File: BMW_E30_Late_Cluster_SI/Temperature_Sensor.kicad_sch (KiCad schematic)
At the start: 30 parts, among them Q11 BC327-16, Q12 BC337-25, Q13 BC337-16, Q14 BC547B, Q15 BC557B, Q17 BC337-25

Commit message: Improved Schematic Readability for SI Board
Added final trace flags for readability of the main page. Also exported a BOM for the SI board
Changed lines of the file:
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@@
 		)
 	)
-	(global_label "IC1_P17"
+	(hierarchical_label "IC1_P19"
 		(shape output)
-		(at 128.27 43.18 0)
-		(fields_autoplaced yes)
+		(at 128.27 57.15 0)
 		(effects
 			(font
@@
 			(justify left)
 		)
-		(property "Intersheetrefs" "${INTERSHEET_REFS}"
-			(at 138.9961 43.18 0)
-			(effects
-				(font
-					(size 1.27 1.27)
-				)
-				(justify left)
-				(hide yes)
+	)
+	(hierarchical_label "IC1_P18"
+		(shape bidirectional)
+		(at 251.46 67.31 0)
+		(effects
+			(font
+				(size 1.27 1.27)
 			)
+			(justify left)
 		)
 	)
-	(global_label "Eng_temp_sensor"
+	(hierarchical_label "Temp_GND"
+		(shape output)
+		(at 124.46 157.48 0)
+		(effects
+			(font
+				(size 1.27 1.27)
+			)
+			(justify left)
+		)
+	)
+	(hierarchical_label "IC1_P23"
+		(shape output)
+		(at 251.46 140.97 0)
+		(effects
+			(font
+				(size 1.27 1.27)
+			)
+			(justify left)
+		)
+	)
+	(hierarchical_label "Temp_+Ub"
+		(shape output)
+		(at 124.46 146.05 0)
+		(effects
+			(font
+				(size 1.27 1.27)
+			)
+			(justify left)
+		)
+	)
+	(hierarchical_label "Eng_temp_sensor"
 		(shape input)
 		(at 68.58 43.18 180)
-		(fields_autoplaced yes)
 		(effects
 			(font
@@
 			(justify right)
 		)
-		(property "Intersheetrefs" "${INTERSHEET_REFS}"
-			(at 49.327 43.18 0)
-			(effects
-				(font
-					(size 1.27 1.27)
-				)
-				(justify right)
-				(hide yes)
-			)
-		)
 	)
-	(global_label "IC1_P18"
+	(hierarchical_label "IC1_P18"
 		(shape input)
 		(at 39.37 148.59 180)
-		(fields_autoplaced yes)
 		(effects
 			(font
@@
 			(justify right)
 		)
-		(property "Intersheetrefs" "${INTERSHEET_REFS}"
-			(at 28.6439 148.59 0)
-			(effects
-				(font
-					(size 1.27 1.27)
-				)
-				(justify right)
-				(hide yes)
-			)
-		)
 	)
-	(global_label "IC3_P7"
-		(shape input)
+	(hierarchical_label "IC3_P7"
+		(shape output)
 		(at 251.46 115.57 0)
-		(fields_autoplaced yes)
 		(effects
 			(font
@@
 			(justify left)
 		)
-		(property "Intersheetrefs" "${INTERSHEET_REFS}"
-			(at 260.9766 115.57 0)
-			(effects
-				(font
-					(size 1.27 1.27)
-				)
-				(justify left)
-				(hide yes)
-			)
-		)
 	)
-	(global_label "IC1_P23"
-		(shape input)
-		(at 251.46 140.97 0)
-		(fields_autoplaced yes)
+	(hierarchical_label "IC1_P17"
+		(shape output)
+		(at 128.27 43.18 0)
 		(effects
 			(font
@@
 			(justify left)
 		)
-		(property "Intersheetrefs" "${INTERSHEET_REFS}"
-			(at 262.1861 140.97 0)
-			(effects
-				(font
-					(size 1.27 1.27)
-				)
-				(justify left)
-				(hide yes)
-			)
-		)
 	)
-	(global_label "IC1_P18"
-		(shape input)
-		(at 251.46 67.31 0)
-		(fields_autoplaced yes)
-		(effects
-			(font
-				(size 1.27 1.27)
-			)
-			(justify left)
-		)
-		(property "Intersheetrefs" "${INTERSHEET_REFS}"
-			(at 262.1861 67.31 0)
-			(effects
-				(font
-					(size 1.27 1.27)
-				)
-				(justify left)
-				(hide yes)
-			)
-		)
-	)
-	(global_label "Temp_+Ub"
-		(shape output)
-		(at 124.46 146.05 0)
-		(fields_autoplaced yes)
-		(effects
-			(font
-				(size 1.27 1.27)
-			)
-			(justify left)
-		)
-		(property "Intersheetrefs" "${INTERSHEET_REFS}"
-			(at 137.3632 146.05 0)
-			(effects
-				(font
-					(size 1.27 1.27)
-				)
-				(justify left)
-				(hide yes)
-			)
-		)
-	)
-	(global_label "Temp_GND"
-		(shape output)
-		(at 124.46 157.48 0)
-		(fields_autoplaced yes)
-		(effects
-			(font
-				(size 1.27 1.27)
-			)
-			(justify left)
-		)
-		(property "Intersheetrefs" "${INTERSHEET_REFS}"
-			(at 137.1818 157.48 0)
-			(effects
-				(font
-					(size 1.27 1.27)
-				)
-				(justify left)
-				(hide yes)
-			)
-		)
-	)
-	(global_label "IC1_P19"
-		(shape output)
-		(at 128.27 57.15 0)
-		(fields_autoplaced yes)
-		(effects
-			(font
-				(size 1.27 1.27)
-			)
-			(justify left)
-		)
-		(property "Intersheetrefs" "${INTERSHEET_REFS}"
-			(at 138.9961 57.15 0)
-			(effects
-				(font
-					(size 1.27 1.27)
-				)
-				(justify left)
-				(hide yes)
-			)
-		)
-	)

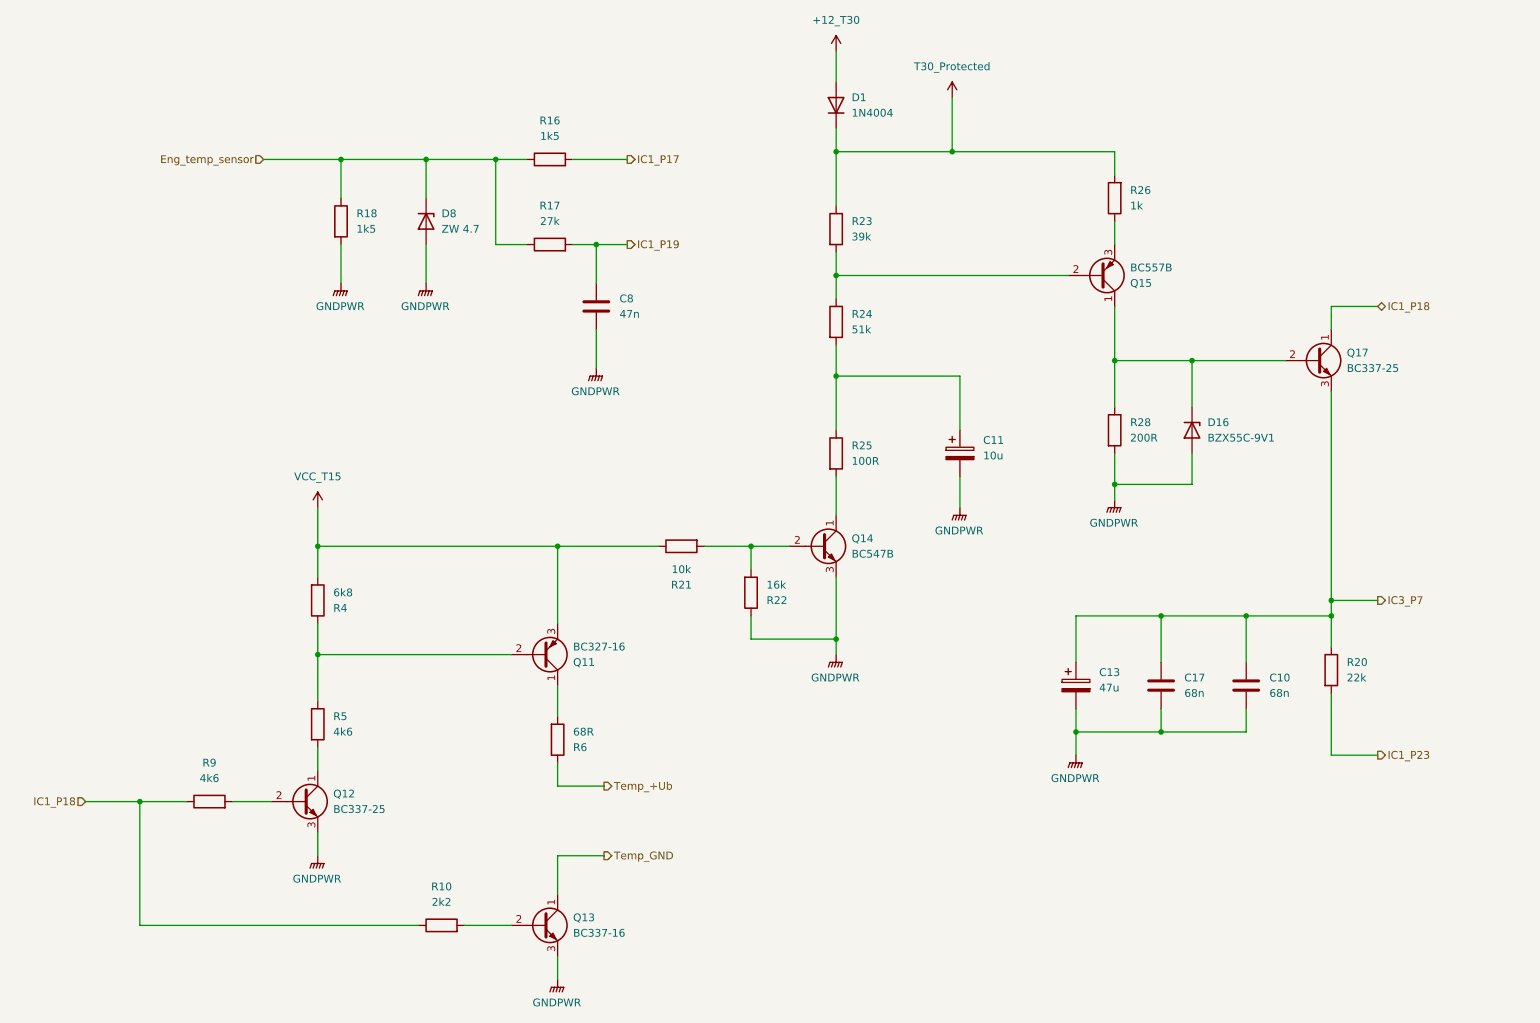
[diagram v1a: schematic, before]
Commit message: SI layout updates
Component positions are mostly complete.
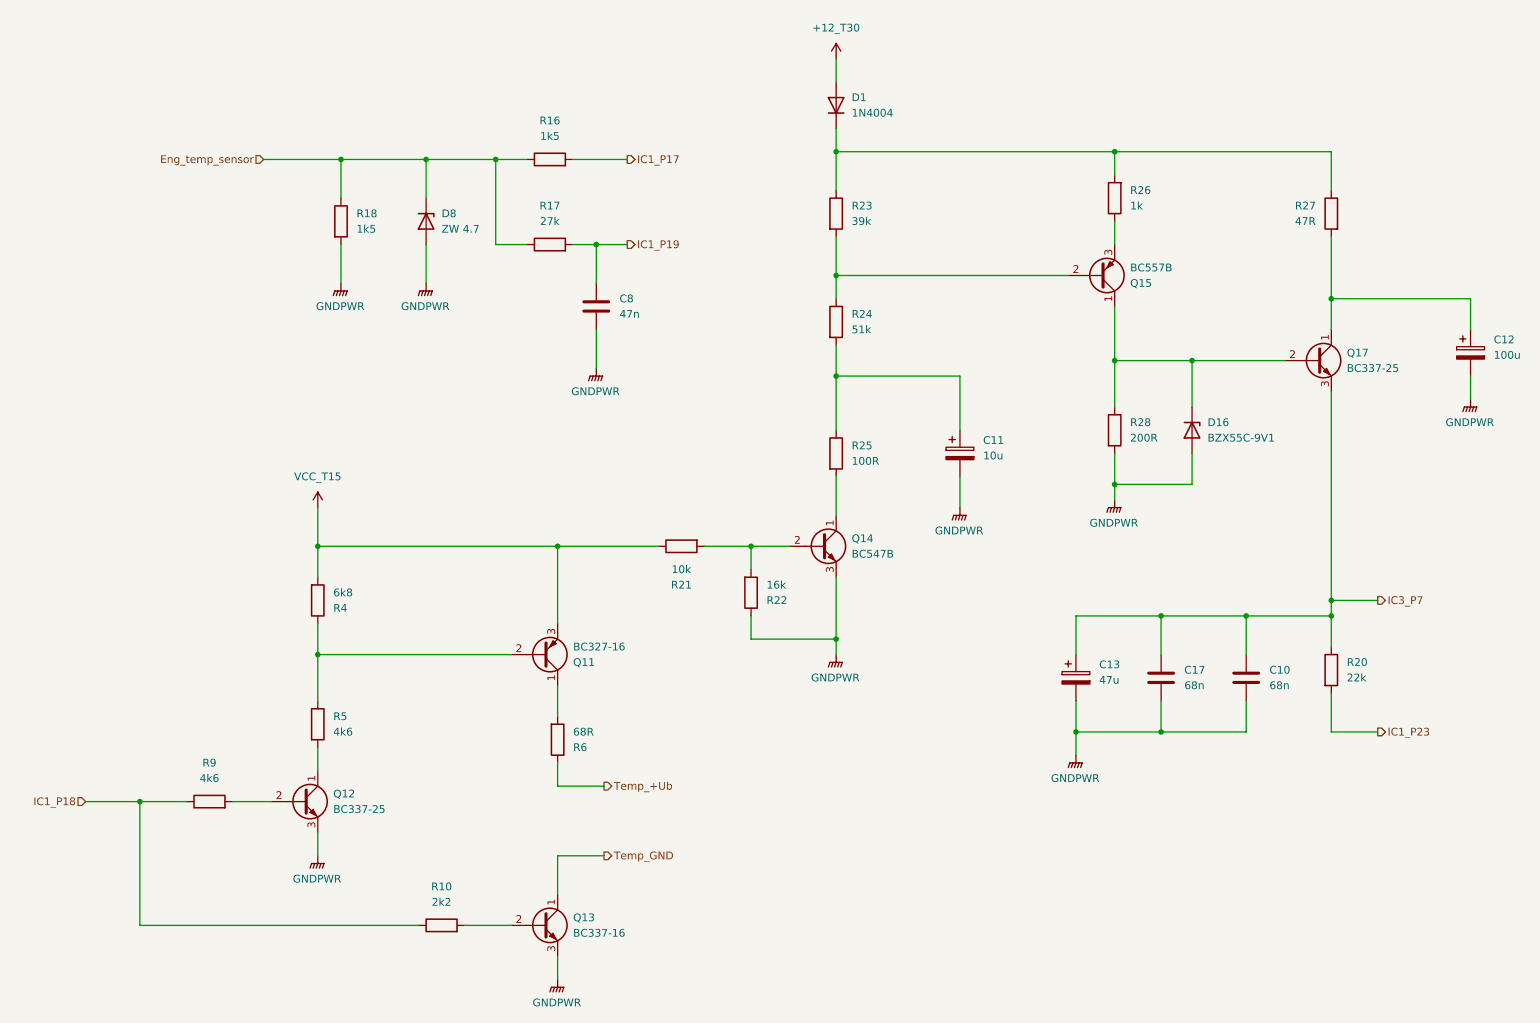
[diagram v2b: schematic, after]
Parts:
- added C12: 100u, Capacitor_THT:CP_Axial_L18.0mm_D6.5mm_P25.00mm_Horizontal, symbol Device:C_Polarized
- added R27: 47R, Resistor_THT:R_Axial_DIN0516_L15.5mm_D5.0mm_P20.32mm_Horizontal, symbol Device:R
- D1: footprint Diode_THT:D_DO-41_SOD81_P10.16mm_Horizontal -> SI_THT:D_Axial_Narrow_L6.7mm_D2.4mm_P9.7mm
- D16, D8: footprint (none) -> SI_THT:D_Axial_Narrow_L6.7mm_D2.4mm_P9.7mm
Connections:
- net GNDPWR: now also C12.2
- net IC1_P18: no longer Q17.1 (C)
- net T30_Protected: no longer names the net of D1.1 (K), R23.1, R26.2
- net T30_Protected: now also R27.1
- new net: C12.1, Q17.1 (C), R27.2
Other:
- moved on the sheet: C10, C13, C17, R23

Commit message: SI Board Layout Updates
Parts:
- R20: footprint Resistor_THT:R_Axial_DIN0207_L6.3mm_D2.5mm_P15.24mm_Horizontal -> SI_THT:R_Axial_DIN0207_L6.3mm_D2.5mm_P22.2mm_Horizontal
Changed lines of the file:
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@@
 			)
 		)
-		(property "Footprint" "Resistor_THT:R_Axial_DIN0207_L6.3mm_D2.5mm_P15.24mm_Horizontal"
+		(property "Footprint" "SI_THT:R_Axial_DIN0207_L6.3mm_D2.5mm_P22.2mm_Horizontal"
 			(at 242.062 127 90)
 			(effects

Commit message: SI Board Layout Complete
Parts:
- removed C10: 68n, Capacitor_THT:C_Disc_D6.0mm_W2.5mm_P5.00mm, symbol Device:C
- C11: footprint Capacitor_THT:CP_Radial_Tantal_D9.0mm_P2.50mm -> Capacitor_THT:CP_Radial_Tantal_D8.0mm_P2.50mm
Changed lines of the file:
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@@
 	)
 	(junction
-		(at 229.87 118.11)
-		(diameter 0)
-		(color 0 0 0 0)
-	)
-	(junction
 		(at 106.68 43.18)
 		(diameter 0)
@@
 	)
 	(junction
-		(at 215.9 137.16)
-		(diameter 0)
-		(color 0 0 0 0)
-	)
-	(junction
 		(at 48.26 148.59)
 		(diameter 0)
@@
 	(wire
 		(pts
-			(xy 229.87 124.46) (xy 229.87 118.11)
-		)
-		(stroke
-			(width 0)
-			(type default)
-		)
-	)
-	(wire
-		(pts
 			(xy 101.6 168.91) (xy 109.22 168.91)
 		)
@@
 	(wire
 		(pts
-			(xy 229.87 118.11) (xy 243.84 118.11)
+			(xy 215.9 118.11) (xy 243.84 118.11)
 		)
 		(stroke
@@
 	(wire
 		(pts
-			(xy 229.87 137.16) (xy 229.87 132.08)
-		)
-		(stroke
-			(width 0)
-			(type default)
-		)
-	)
-	(wire
-		(pts
 			(xy 81.28 43.18) (xy 81.28 49.53)
 		)
@@
 	(wire
 		(pts
-			(xy 229.87 118.11) (xy 215.9 118.11)
-		)
-		(stroke
-			(width 0)
-			(type default)
-		)
-	)
-	(wire
-		(pts
 			(xy 81.28 43.18) (xy 95.25 43.18)
 		)
@@
 	(wire
 		(pts
-			(xy 215.9 137.16) (xy 229.87 137.16)
-		)
-		(stroke
-			(width 0)
-			(type default)
-		)
-	)
-	(wire
-		(pts
 			(xy 93.98 168.91) (xy 48.26 168.91)
 		)
@@
 			)
 		)
-		(property "Footprint" "Capacitor_THT:CP_Radial_Tantal_D9.0mm_P2.50mm"
+		(property "Footprint" "Capacitor_THT:CP_Radial_Tantal_D8.0mm_P2.50mm"
 			(at 183.8452 95.25 0)
 			(effects
@@
 					(unit 1)
 				)
-			)
-		)
-	)
-	(symbol
-		(lib_id "Device:C")
-		(at 229.87 128.27 0)
-		(unit 1)
-		(exclude_from_sim no)
-		(in_bom yes)
-		(on_board yes)
-		(dnp no)
-		(fields_autoplaced yes)
-		(property "Reference" "C10"
-			(at 233.68 126.9999 0)
-			(effects
-				(font
-					(size 1.27 1.27)
-				)
-				(justify left)
-			)
-		)
-		(property "Value" "68n"
-			(at 233.68 129.5399 0)
-			(effects
-				(font
-					(size 1.27 1.27)
-				)
-				(justify left)
-			)
-		)
-		(property "Footprint" "Capacitor_THT:C_Disc_D6.0mm_W2.5mm_P5.00mm"
-			(at 230.8352 132.08 0)
-			(effects
-				(font
-					(size 1.27 1.27)
-				)
-				(hide yes)
-			)
-		)
-		(property "Datasheet" "~"
-			(at 229.87 128.27 0)
-			(effects
-				(font
-					(size 1.27 1.27)
-				)
-				(hide yes)
-			)
-		)
-		(property "Description" "Unpolarized capacitor"
-			(at 229.87 128.27 0)
-			(effects
-				(font
-					(size 1.27 1.27)
-				)
-				(hide yes)
-			)
-		)
-		(pin "2"
-		)
-		(pin "1"
-		)
-		(instances
-			(project "BMW_E30_Late_Cluster_SI"
-				(path "/00d578f4-1582-4e4e-9a07-e5462d38fb61/84ca9cc6-3e51-42c7-8f6d-11ef7495b962"
-					(reference "C10")
-					(unit 1)
-				)

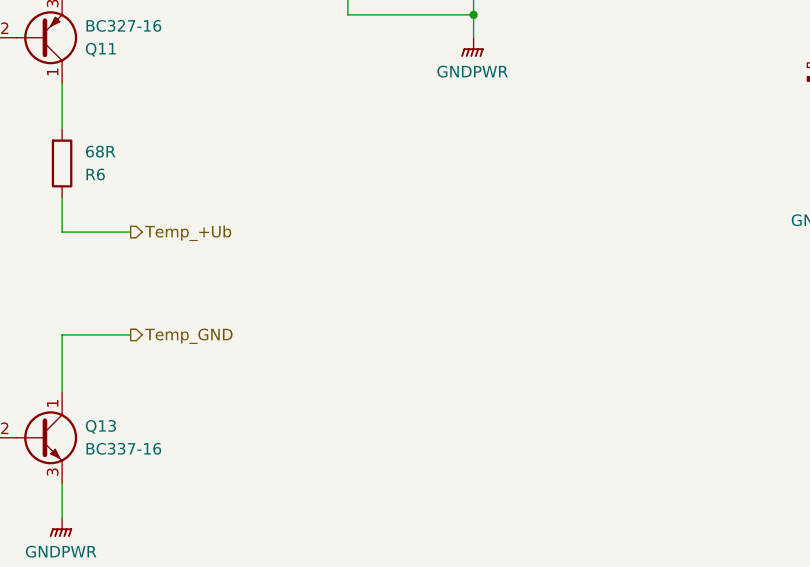
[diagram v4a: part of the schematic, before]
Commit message: Readability Improvements
Organized the schematic for better readability, also made a few minor adjustments to the layout for simplicity.
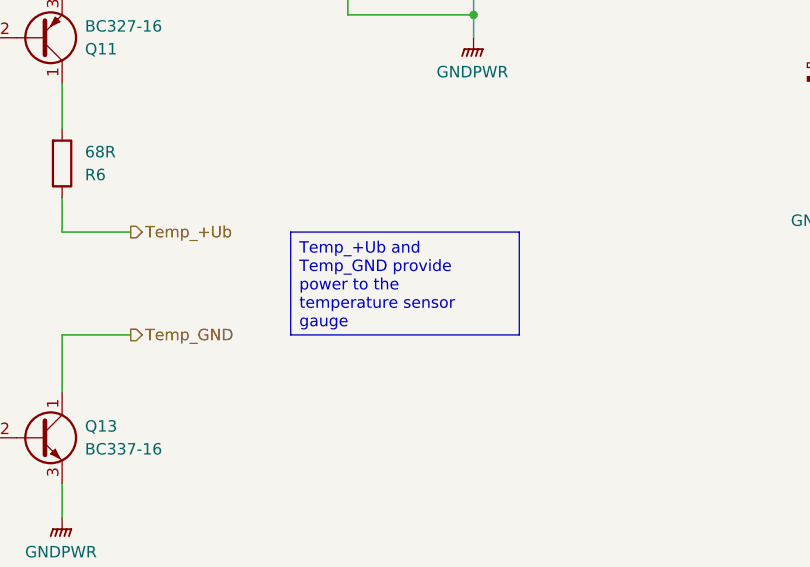
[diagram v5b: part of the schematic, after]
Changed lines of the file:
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@@
 		(company "Reagan Ansel")
+	)
+	(text_box "Temp_+Ub and Temp_GND provide power to the temperature sensor gauge"
+		(exclude_from_sim no)
+		(at 142.24 146.05 0)
+		(size 25.4 11.43)
+		(margins 0.9525 0.9525 0.9525 0.9525)
+		(stroke
+			(width 0)
+			(type solid)
+		)
+		(fill
+			(type color)
+			(color 255 229 191 1)
+		)
+		(effects
+			(font
+				(size 1.27 1.27)
+				(thickness 0.1588)
+			)
+			(justify left top)
+		)
 	)
 	(junction

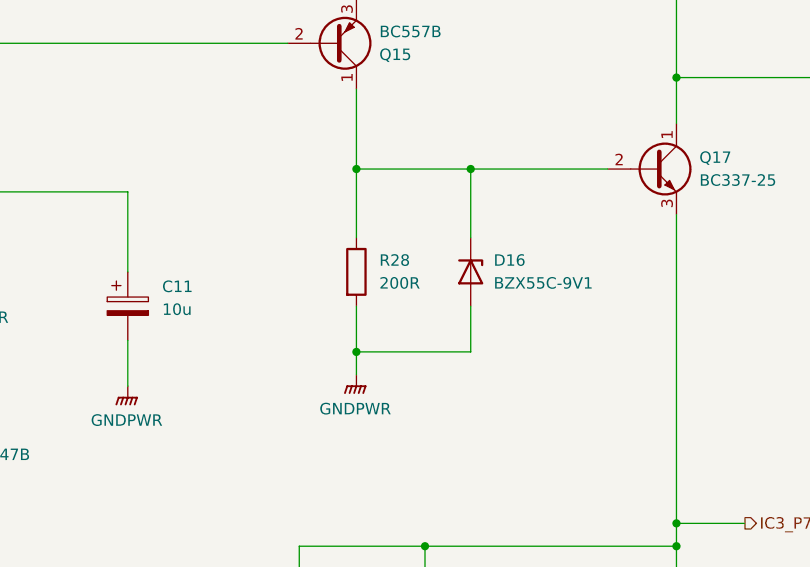
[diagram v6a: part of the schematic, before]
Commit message: Updated Resistor Value
R28 Value was incorrect, changed from 200R to 200k ohms
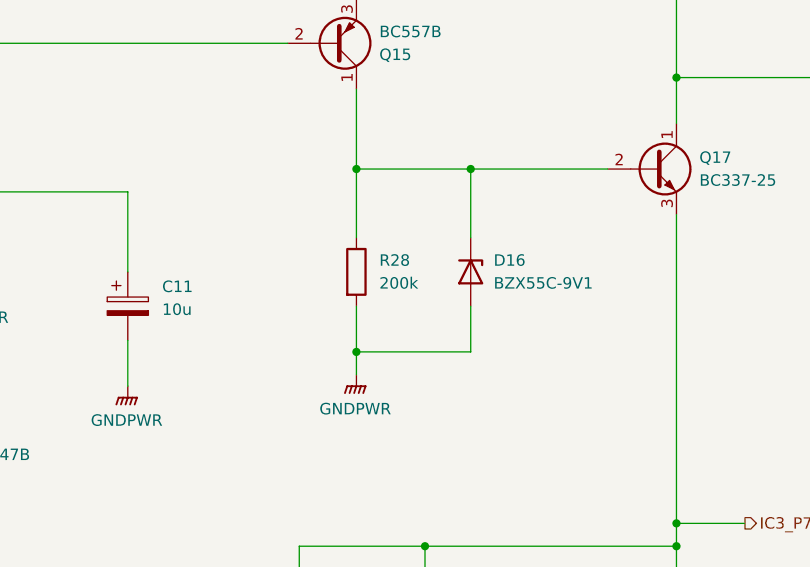
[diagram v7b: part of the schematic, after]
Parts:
- R28: value 200R -> 200k
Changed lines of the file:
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@@
 			)
 		)
-		(property "Value" "200R"
+		(property "Value" "200k"
 			(at 210.82 88.8999 0)
 			(effects
